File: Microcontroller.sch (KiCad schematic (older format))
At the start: 29 parts, among them J3 USB_B, J4 SWD, J5 DEBUG, U3 STM32F401VETx, U4 USBUF02W6, Y1 8MHz

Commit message: Added git ignore, updated part info for USB socket
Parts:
- J3: Cena 2.9560 -> 2.73; Link https://www.tme.eu/pl/details/2411-02/zlacza-usb-i-ieee1394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 -> https://pl.farnell.com/multicomp/mc32597/usb-2-0-type-b-rec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; Model 2411 02 -> MC32597; Opis Gniazdo; USB B; na PCB; THT; PIN: 4; kątowe 90°; V: USB 2.0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 -> Złącze USB, USB typu B, USB 2.0, Gniazdo, 4 tory/-ów, Monta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; Producent LUMBERG -> MULTICOMP PRO
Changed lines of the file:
@@
 F 2 "Connector_USB:USB_B_TE_5787834_Vertical" H 7750 1650 50  0001 C CNN
 F 3 " ~" H 7750 1650 50  0001 C CNN
-F 4 "2.9560" H 7600 1700 50  0001 C CNN "Cena"
-F 5 "https://www.tme.eu/pl/details/2411-02/zlacza-usb-i-ieee1394/lumberg/2411-02/" H 7600 1700 50  0001 C CNN "Link"
-F 6 "2411 02" H 7600 1700 50  0001 C CNN "Model"
-F 7 "Gniazdo; USB B; na PCB; THT; PIN: 4; kątowe 90°; V: USB 2.0; biały" H 7600 1700 50  0001 C CNN "Opis"
-F 8 "LUMBERG" H 7600 1700 50  0001 C CNN "Producent"
+F 4 "2.73" H 7600 1700 50  0001 C CNN "Cena"
+F 5 "https://pl.farnell.com/multicomp/mc32597/usb-2-0-type-b-receptacle-th/dp/1696538?MER=sy-me-pd-mi-alte" H 7600 1700 50  0001 C CNN "Link"
+F 6 "MC32597" H 7600 1700 50  0001 C CNN "Model"
+F 7 "Złącze USB, USB typu B, USB 2.0, Gniazdo, 4 tory/-ów, Montaż przewlekany, Pionowe " H 7600 1700 50  0001 C CNN "Opis"
+F 8 "MULTICOMP PRO" H 7600 1700 50  0001 C CNN "Producent"
 F 9 "THT" H 7600 1700 50  0001 C CNN "Typ"
 	1    7600 1700

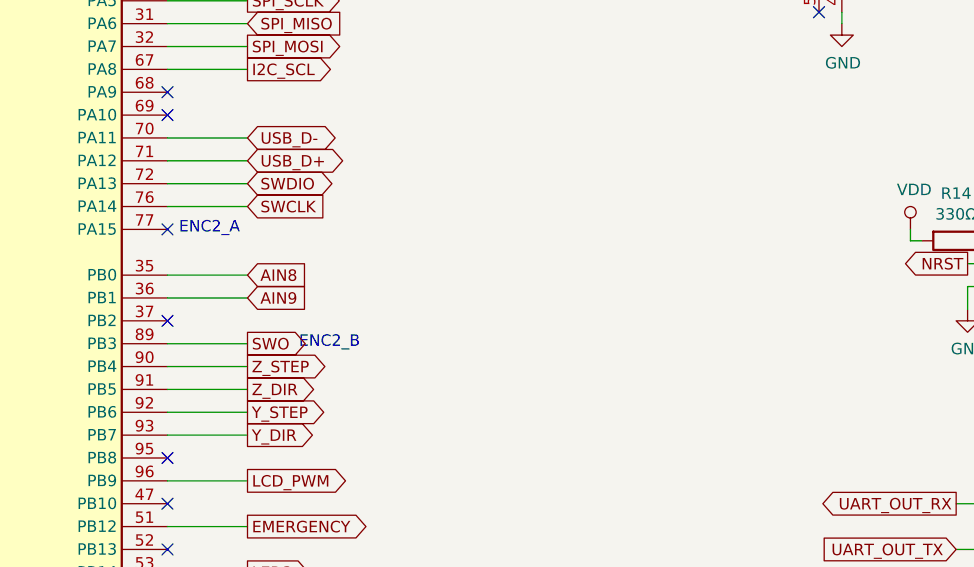
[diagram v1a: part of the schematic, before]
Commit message: Added rotary encoder input
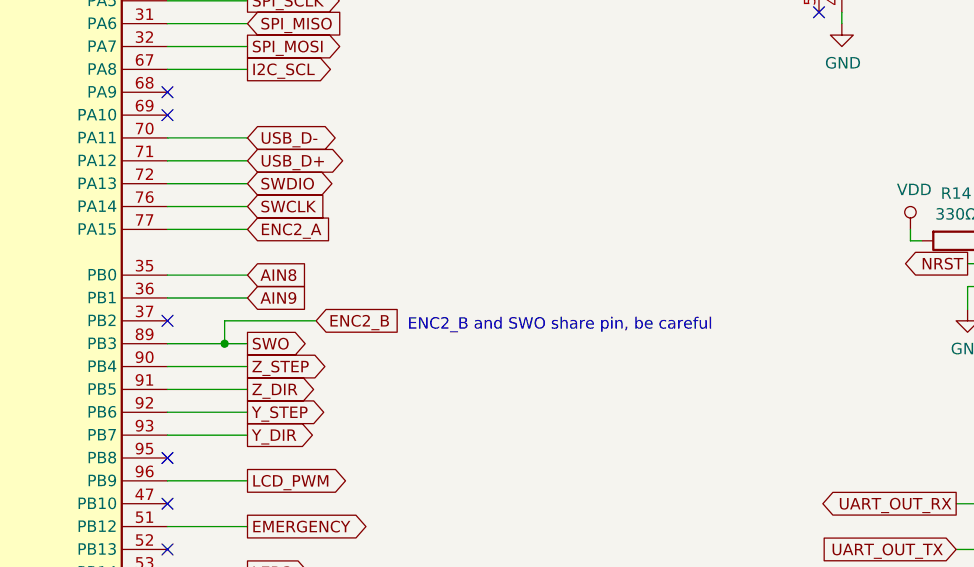
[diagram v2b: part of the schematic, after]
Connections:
- net ENC2_A: now reaches U3.77 (PA15)
- net SWO renamed ENC2_B
- no-connect marks 19 -> 18
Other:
- note added: "ENC2_B and SWO share pin, be careful"
- note removed: "ENC2_A"
- note removed: "ENC2_B"
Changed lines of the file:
@@
 SWO
 Wire Wire Line
-	4650 3550 5000 3550
-NoConn ~ 4650 3050
-Text Notes 4700 3075 0    50   ~ 0
-ENC2_A
-Text Notes 5225 3575 0    50   ~ 0
-ENC2_B
+	4650 3550 4900 3550
 Wire Wire Line
 	2750 2050 2750 2250
@@
 	0    1    1    0
 $EndComp
+Text GLabel 5000 3050 2    50   Input ~ 0
+ENC2_A
+Text GLabel 5300 3450 2    50   Input ~ 0
+ENC2_B
+Wire Wire Line
+	4650 3050 5000 3050
+Wire Wire Line
+	4900 3550 4900 3450
+Wire Wire Line
+	4900 3450 5300 3450
+Connection ~ 4900 3550
+Wire Wire Line
+	4900 3550 5000 3550
+Text Notes 5700 3500 0    50   ~ 0
+ENC2_B and SWO share pin, be careful
 $EndSCHEMATC

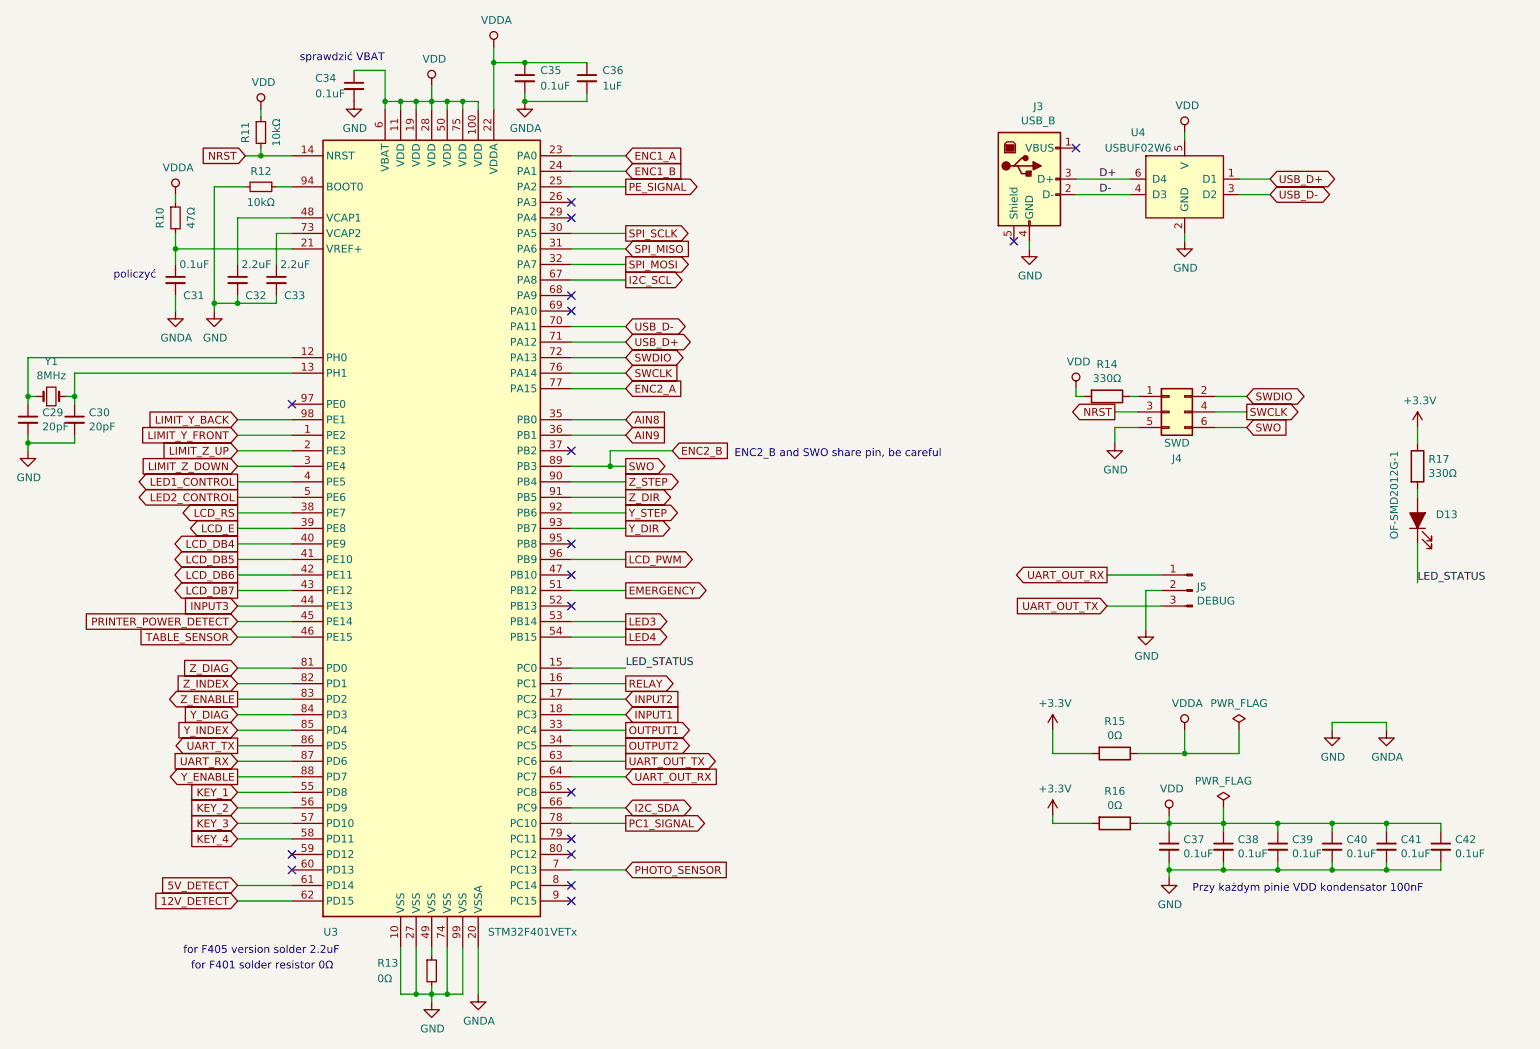
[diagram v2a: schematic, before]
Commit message: Modify pin attribute, routing keys input
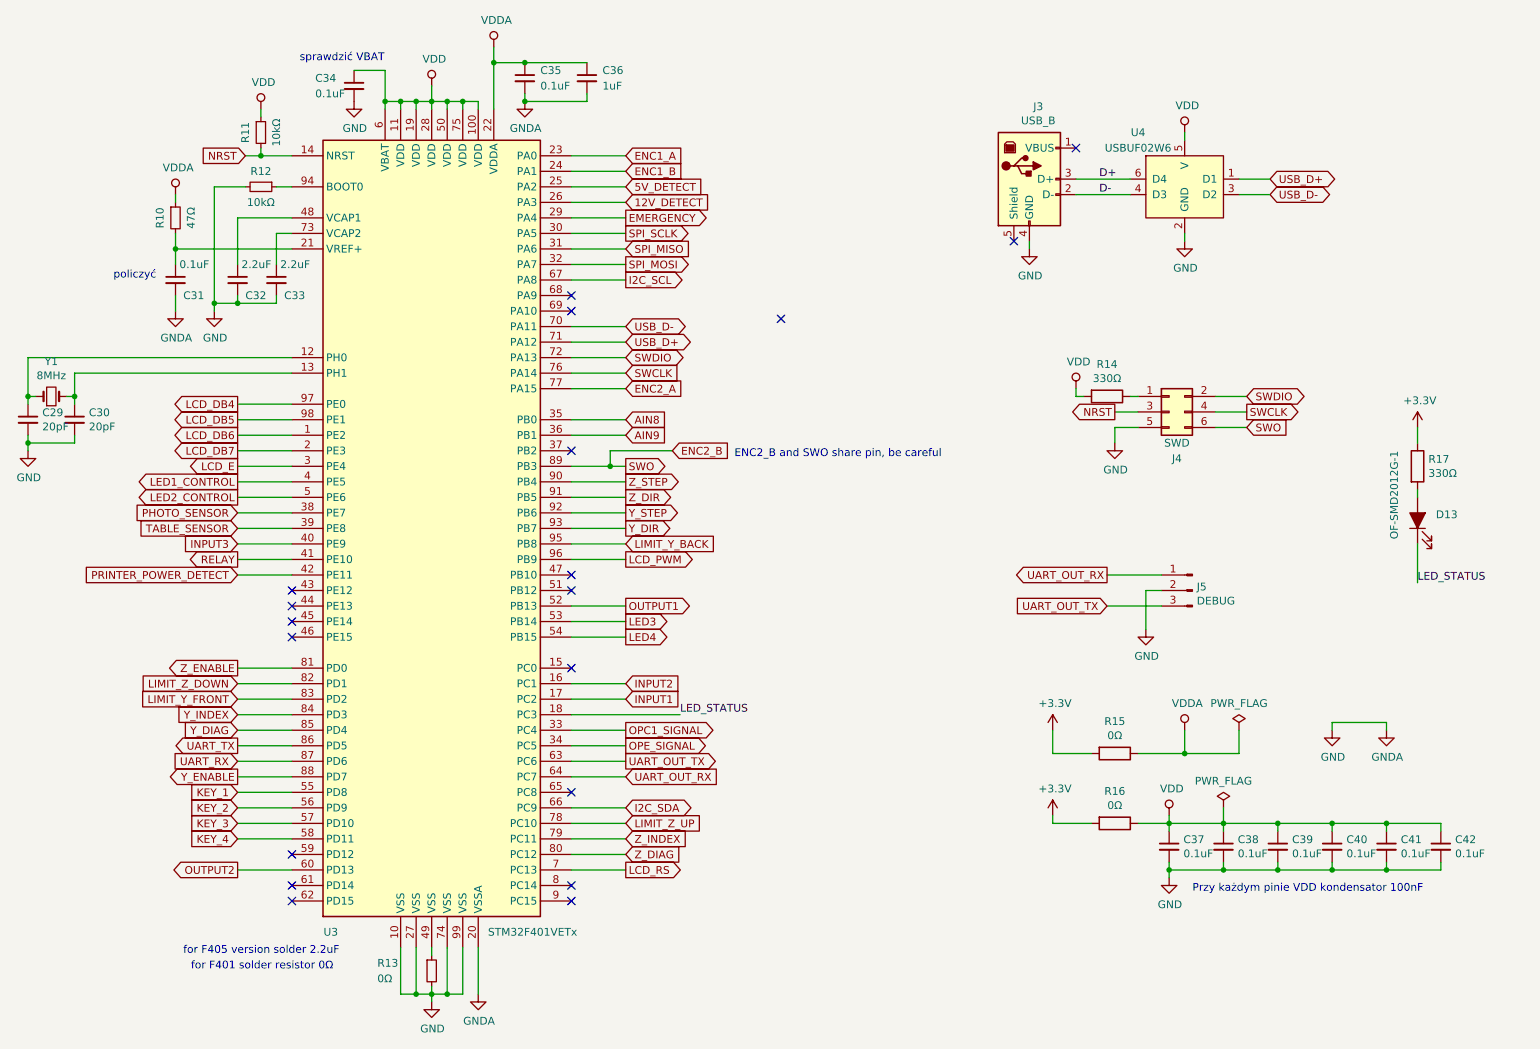
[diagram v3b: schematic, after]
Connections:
- net PC1_SIGNAL is gone; now on net LIMIT_Z_UP: U3.78 (PC10)
- net PE_SIGNAL is gone; now on net 5V_DETECT: U3.25 (PA2)
- net 12V_DETECT: now also U3.26 (PA3); no longer U3.62 (PD15)
- net 5V_DETECT: no longer U3.61 (PD14)
- net EMERGENCY: now also U3.29 (PA4); no longer U3.51 (PB12)
- net INPUT1: now also U3.17 (PC2); no longer U3.18 (PC3)
- net INPUT2: now also U3.16 (PC1); no longer U3.17 (PC2)
- net INPUT3: now also U3.40 (PE9); no longer U3.44 (PE13)
- net LCD_DB4: now also U3.97 (PE0); no longer U3.40 (PE9)
- net LCD_DB5: now also U3.98 (PE1); no longer U3.41 (PE10)
- net LCD_DB6: now also U3.1 (PE2); no longer U3.42 (PE11)
- net LCD_DB7: now also U3.2 (PE3); no longer U3.43 (PE12)
- net LCD_E: now also U3.3 (PE4); no longer U3.39 (PE8)
- net LCD_RS: now also U3.7 (PC13); no longer U3.38 (PE7)
- net LED_STATUS: now also U3.18 (PC3); no longer U3.15 (PC0)
- net LIMIT_Y_BACK: now also U3.95 (PB8); no longer U3.98 (PE1)
- net LIMIT_Y_FRONT: now also U3.83 (PD2); no longer U3.1 (PE2)
- net LIMIT_Z_DOWN: now also U3.82 (PD1); no longer U3.3 (PE4)
- net LIMIT_Z_UP: no longer U3.2 (PE3)
- net OUTPUT1: now also U3.52 (PB13); no longer U3.33 (PC4)
- net OUTPUT2: now also U3.60 (PD13); no longer U3.34 (PC5)
- net PHOTO_SENSOR: now also U3.38 (PE7); no longer U3.7 (PC13)
- net PRINTER_POWER_DETECT: now also U3.42 (PE11); no longer U3.45 (PE14)
- net RELAY: now also U3.41 (PE10); no longer U3.16 (PC1)
- net TABLE_SENSOR: now also U3.39 (PE8); no longer U3.46 (PE15)
- net Y_DIAG: now also U3.85 (PD4); no longer U3.84 (PD3)
- net Y_INDEX: now also U3.84 (PD3); no longer U3.85 (PD4)
- net Z_DIAG: now also U3.80 (PC12); no longer U3.81 (PD0)
- net Z_ENABLE: now also U3.81 (PD0); no longer U3.83 (PD2)
- net Z_INDEX: now also U3.79 (PC11); no longer U3.82 (PD1)
- new net OPC1_SIGNAL: U3.33 (PC4)
- new net OPE_SIGNAL: U3.34 (PC5)
- no-connect marks 18 -> 19
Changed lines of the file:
@@
 Text GLabel 2500 5550 0    50   Output ~ 0
 Y_ENABLE
-Text GLabel 2500 5050 0    50   Output ~ 0
+Text GLabel 2500 4850 0    50   Output ~ 0
 Z_ENABLE
-Text GLabel 5000 4350 2    50   Output ~ 0
+Text GLabel 5000 1950 2    50   Output ~ 0
 EMERGENCY
-Text GLabel 2500 4050 0    50   Output ~ 0
+Text GLabel 2500 3150 0    50   Output ~ 0
 LCD_DB4
-Text GLabel 2500 4150 0    50   Output ~ 0
+Text GLabel 2500 3250 0    50   Output ~ 0
 LCD_DB5
-Text GLabel 2500 4250 0    50   Output ~ 0
+Text GLabel 2500 3350 0    50   Output ~ 0
 LCD_DB6
-Text GLabel 2500 4350 0    50   Output ~ 0
+Text GLabel 2500 3450 0    50   Output ~ 0
 LCD_DB7
-Text GLabel 2500 3950 0    50   Output ~ 0
-LCD_E
-Text GLabel 2500 3850 0    50   Output ~ 0
+Text GLabel 5000 6150 2    50   Output ~ 0
 LCD_RS
 Text GLabel 5000 4150 2    50   Output ~ 0
@@
 Text GLabel 5000 2250 2    50   Output ~ 0
 SPI_MOSI
-Text GLabel 2500 3250 0    50   Input ~ 0
+Text GLabel 5000 4050 2    50   Input ~ 0
 LIMIT_Y_BACK
-Text GLabel 2500 3550 0    50   Input ~ 0
+Text GLabel 2500 4950 0    50   Input ~ 0
 LIMIT_Z_DOWN
-Text GLabel 2500 3450 0    50   Input ~ 0
+Text GLabel 5000 5850 2    50   Input ~ 0
 LIMIT_Z_UP
-Text GLabel 2500 3350 0    50   Input ~ 0
+Text GLabel 2500 5050 0    50   Input ~ 0
 LIMIT_Y_FRONT
-Text GLabel 5000 1750 2    50   Output ~ 0
-PE_SIGNAL
-Text GLabel 5000 6150 2    50   Input ~ 0
+Text GLabel 5000 5350 2    50   Output ~ 0
+OPE_SIGNAL
+Text GLabel 2500 3850 0    50   Input ~ 0
 PHOTO_SENSOR
 Text GLabel 5000 3850 2    50   Output ~ 0
@@
 Text GLabel 2500 5350 0    50   Output ~ 0
 UART_TX
+Text GLabel 2500 5150 0    50   Input ~ 0
+Y_INDEX
 Text GLabel 2500 5250 0    50   Input ~ 0
-Y_INDEX
-Text GLabel 2500 5150 0    50   Input ~ 0
 Y_DIAG
 Text GLabel 5000 3650 2    50   Output ~ 0
@@
 Text GLabel 5000 3750 2    50   Output ~ 0
 Z_DIR
-Text GLabel 2500 4950 0    50   Input ~ 0
+Text GLabel 5000 5950 2    50   Input ~ 0
 Z_INDEX
-Text GLabel 2500 4850 0    50   Input ~ 0
+Text GLabel 5000 6050 2    50   Input ~ 0
 Z_DIAG
 Wire Wire Line
@@
 	4650 4150 5000 4150
 Wire Wire Line
-	5000 4350 4650 4350
-Wire Wire Line
 	2500 3850 2850 3850
 Wire Wire Line
@@
 	2500 4250 2850 4250
 Wire Wire Line
-	2850 4350 2500 4350
-Wire Wire Line
 	5000 1750 4650 1750
 Wire Wire Line
@@
 Wire Wire Line
 	4650 6150 5000 6150
-Wire Wire Line
-	2500 4550 2850 4550
-Text GLabel 2500 4550 0    50   Input ~ 0
+Text GLabel 2500 4250 0    50   Input ~ 0
 PRINTER_POWER_DETECT
 $Comp
@@
 Text GLabel 9000 3200 2    50   Output ~ 0
 SWCLK
-Text GLabel 2500 4650 0    50   Input ~ 0
+Text GLabel 2500 3950 0    50   Input ~ 0
 TABLE_SENSOR
-Text Label 5000 4850 0    50   ~ 0
+Text Label 5350 5150 0    50   ~ 0
 LED_STATUS
-Wire Wire Line
-	4650 4850 5000 4850
-Wire Wire Line
-	2500 4650 2850 4650
 Wire Wire Line
 	8100 4250 8450 4250
@@
 	1    0    0    -1
 $EndComp
-NoConn ~ 2850 3150
 NoConn ~ 4650 2450
 NoConn ~ 4650 2550
-NoConn ~ 4650 1850
-NoConn ~ 4650 1950
 NoConn ~ 4650 3450
-NoConn ~ 4650 4050
 NoConn ~ 4650 4250
-NoConn ~ 4650 4450
 NoConn ~ 4650 5650
-NoConn ~ 4650 5950
-NoConn ~ 4650 6050
 NoConn ~ 4650 6350
 NoConn ~ 4650 6250
-NoConn ~ 2850 6150
-NoConn ~ 2850 6050
 Wire Wire Line
 	3550 1200 3450 1200
@@
 Text GLabel 5000 2650 2    50   BiDi ~ 0
 USB_D-
-Text GLabel 2500 4450 0    50   Input ~ 0
+Text GLabel 2500 4050 0    50   Input ~ 0
 INPUT3
+Text GLabel 5000 4450 2    50   Output ~ 0
+OUTPUT1
+Text GLabel 2500 6150 0    50   Output ~ 0
+OUTPUT2
+Text GLabel 5000 5050 2    50   Input ~ 0
+INPUT1
+Text GLabel 5000 4950 2    50   Input ~ 0
+INPUT2
+Wire Wire Line
+	5000 5050 4650 5050
+Wire Wire Line
+	4650 5150 5350 5150
+Wire Wire Line
+	5000 5250 4650 5250
+Wire Wire Line
+	4650 5350 5000 5350
+Text GLabel 2500 4150 0    50   Output ~ 0
+RELAY
+Wire Wire Line
+	4650 4950 5000 4950
+Text GLabel 5000 1750 2    50   Input ~ 0
+5V_DETECT
+Text GLabel 5000 1850 2    50   Input ~ 0
+12V_DETECT
 Text GLabel 5000 5250 2    50   Output ~ 0
-OUTPUT1
-Text GLabel 5000 5350 2    50   Output ~ 0
-OUTPUT2
-Text GLabel 5000 5150 2    50   Input ~ 0
-INPUT1
-Text GLabel 5000 5050 2    50   Input ~ 0
-INPUT2
-Wire Wire Line
-	5000 5050 4650 5050
-Wire Wire Line
-	4650 5150 5000 5150
-Wire Wire Line
-	5000 5250 4650 5250
-Wire Wire Line
-	4650 5350 5000 5350
-Wire Wire Line
-	2500 4450 2850 4450
-Text GLabel 5000 4950 2    50   Output ~ 0
-RELAY
-Wire Wire Line
-	4650 4950 5000 4950
-Text GLabel 2500 6250 0    50   Input ~ 0
-5V_DETECT
-Text GLabel 2500 6350 0    50   Input ~ 0
-12V_DETECT
-Wire Wire Line
-	2500 6250 2850 6250
-Wire Wire Line
-	2850 6350 2500 6350
-Text GLabel 5000 5850 2    50   Output ~ 0
-PC1_SIGNAL
+OPC1_SIGNAL
 Wire Wire Line
 	4650 5850 5000 5850
@@
 Text Notes 5700 3500 0    50   ~ 0
 ENC2_B and SWO share pin, be careful
+Wire Wire Line
+	2500 3150 2850 3150
+Wire Wire Line
+	4650 4050 5000 4050
+Text GLabel 2500 3550 0    50   Output ~ 0
+LCD_E
+Wire Wire Line
+	4650 5950 5000 5950
+Wire Wire Line
+	5000 6050 4650 6050
+NoConn ~ 4650 4850
+Wire Wire Line
+	4650 1850 5000 1850
+Wire Wire Line
+	4650 1950 5000 1950
+Wire Wire Line
+	2500 6150 2850 6150
+NoConn ~ 4650 4350
+NoConn ~ 2850 4350
+NoConn ~ 2850 4450
+NoConn ~ 2850 4550
+NoConn ~ 2850 4650
+NoConn ~ 2850 6250
+NoConn ~ 2850 6350
+Wire Wire Line
+	4650 4450 5000 4450
+NoConn ~ 2850 6050
+NoConn ~ 6000 2600
 $EndSCHEMATC
